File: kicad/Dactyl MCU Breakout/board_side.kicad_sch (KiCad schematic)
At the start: 19 parts, among them J11 Columns, J12 Thumbs, J13 Rows, J14 Extrernal, J15 Split, J16 JST, J9 Display, SW4 LED, SW5 Reset, SW6 Battery, U3 Nice!Nano/2040, U4 74HC595

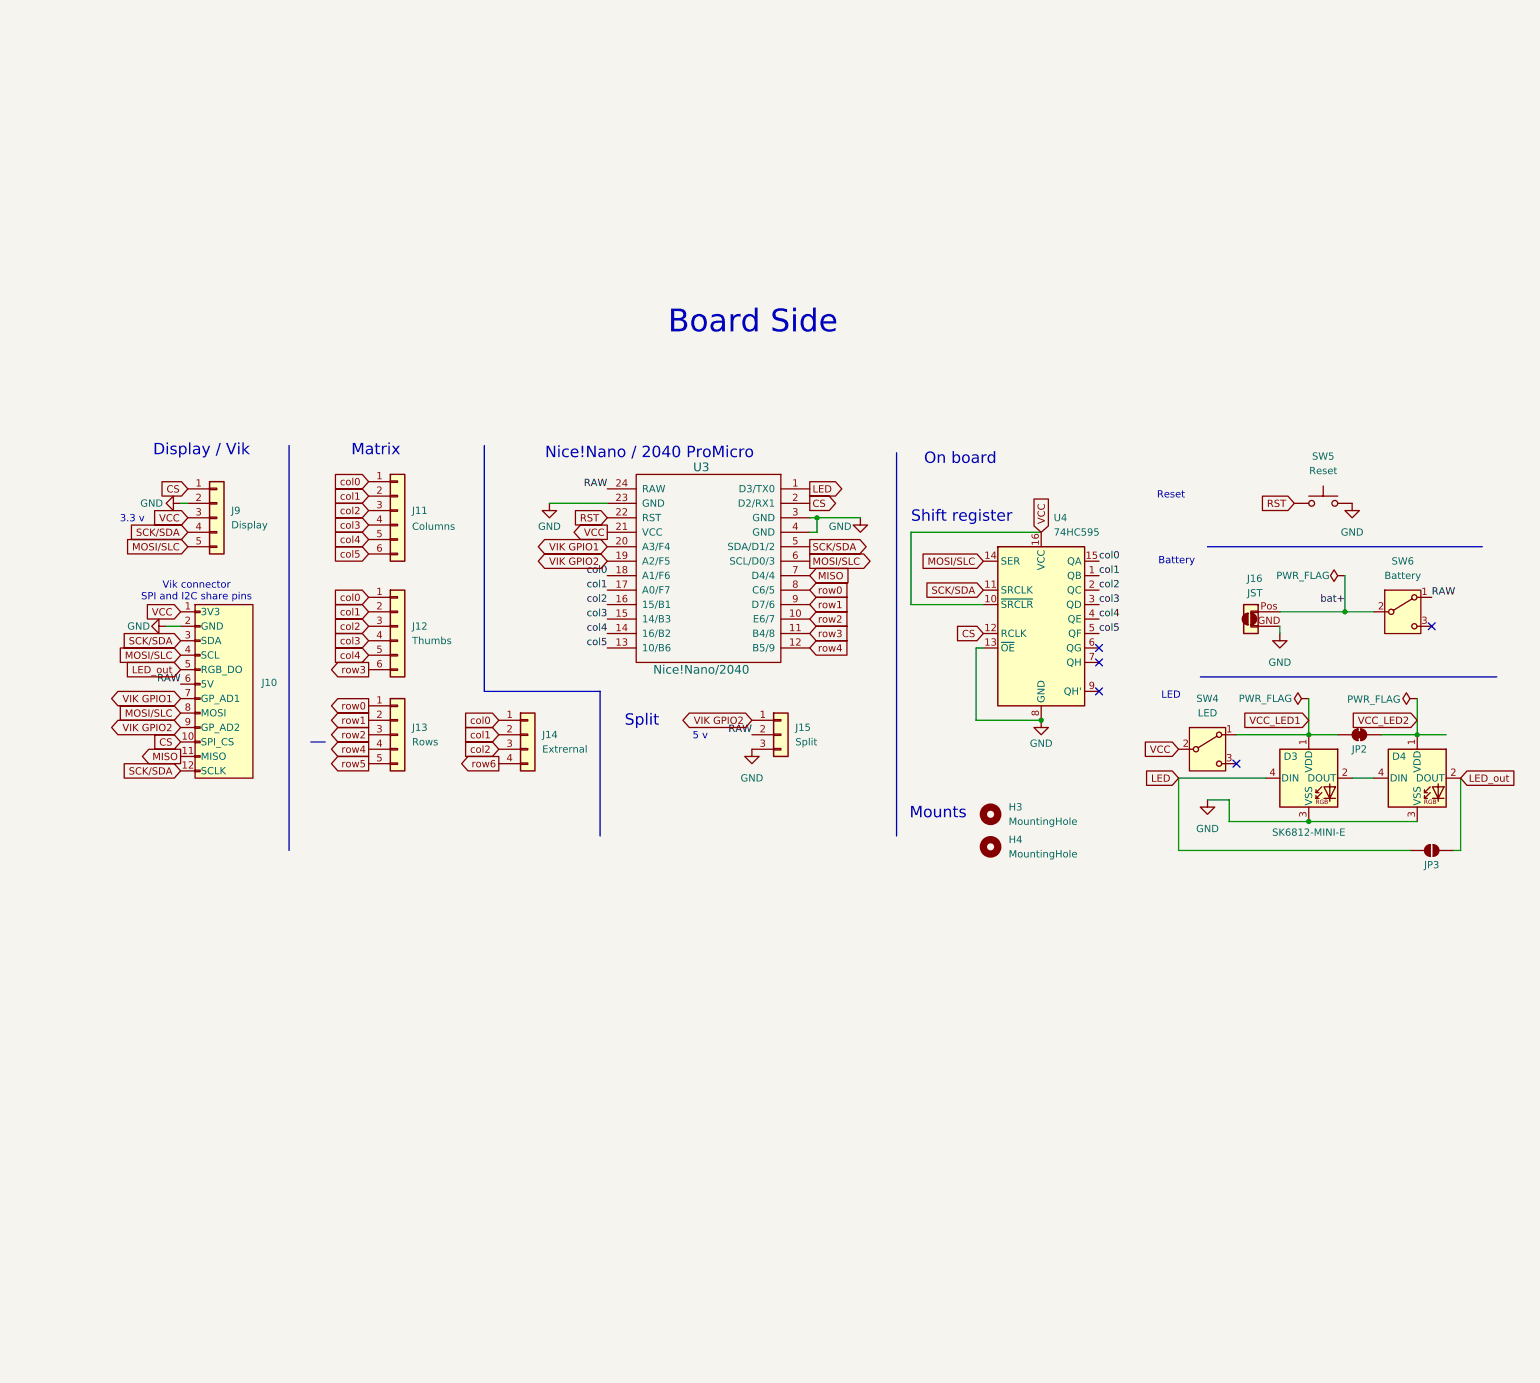
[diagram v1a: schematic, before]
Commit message: feat: bus SPI0, mum/2040 split steal form Vik
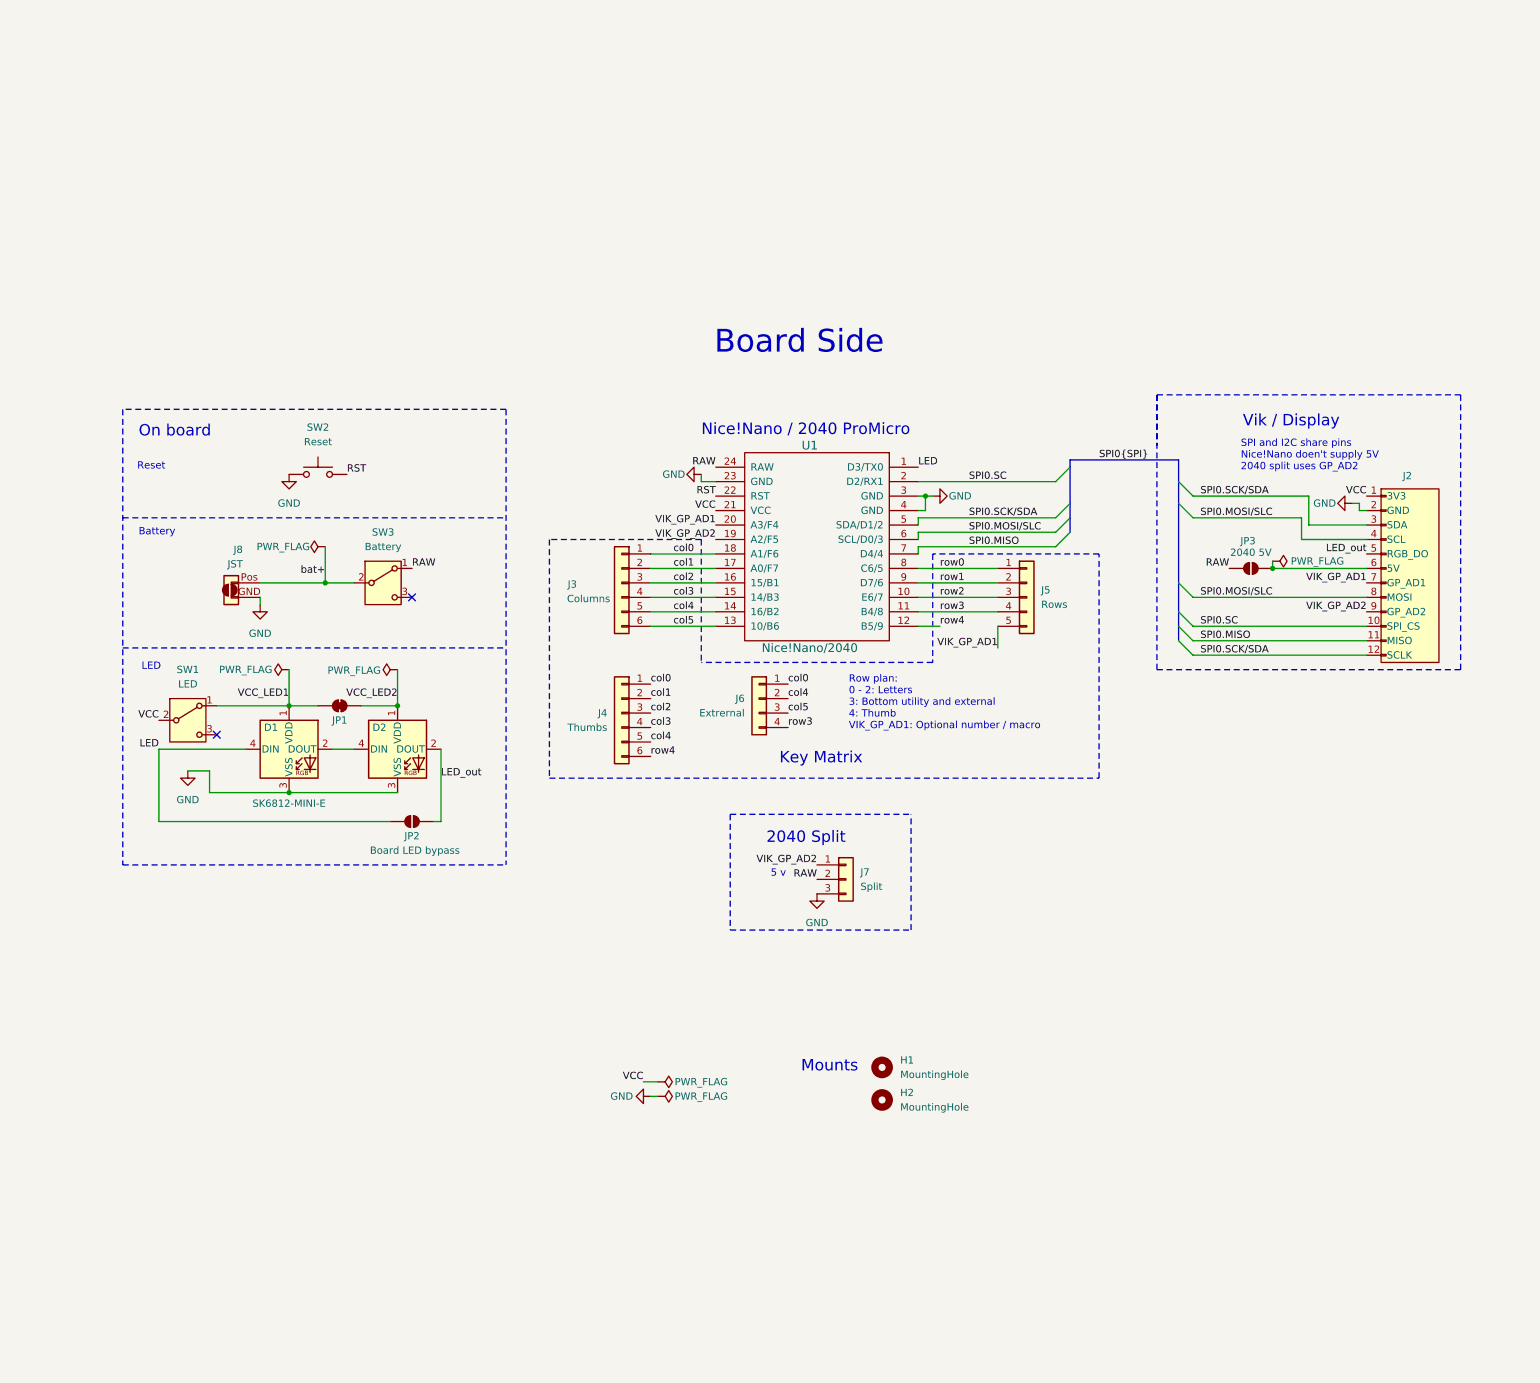
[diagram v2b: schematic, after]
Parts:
- removed D3, D4: SK6812-MINI-E, Dactyl:SK6812-MINI-E-Dog2, symbol Dactyl:SK6812-MINI-E
- removed H3, H4: MountingHole, MountingHole:MountingHole_3.2mm_M3_DIN965_Pad, symbol Mechanical:MountingHole
- removed J10: ~, symbol Dactyl:vik-keyboard-connector
- removed J11: Columns, Connector_PinHeader_2.54mm:PinHeader_1x06_P2.54mm_Vertical, symbol Connector_Generic:Conn_01x06
- removed J12: Thumbs, Connector_PinHeader_2.54mm:PinHeader_1x06_P2.54mm_Vertical, symbol Connector_Generic:Conn_01x06
- removed J13: Rows, Connector_PinHeader_2.54mm:PinHeader_1x05_P2.54mm_Vertical, symbol Connector_Generic:Conn_01x05
- removed J14: Extrernal, Connector_PinHeader_2.54mm:PinHeader_1x04_P2.54mm_Vertical, symbol Connector_Generic:Conn_01x04
- removed J15: Split, Connector_PinHeader_2.54mm:PinHeader_1x03_P2.54mm_Vertical, symbol Connector_Generic:Conn_01x03
- removed J16: JST, Dactyl:JST_PH_S2B-PH-K_1x02_P2.00mm_Horizontal, symbol Dactyl:Conn_01x02_Jump_Two_Side
- removed J9: Display, Connector_PinHeader_2.54mm:PinHeader_1x05_P2.54mm_Vertical, symbol Connector_Generic:Conn_01x05
- removed JP2: LED2 cutoff, Jumper:SolderJumper-2_P1.3mm_Bridged_RoundedPad1.0x1.5mm, symbol Jumper:SolderJumper_2_Bridged
- removed SW4: LED, Dactyl:SW_SPDT_JS202011AQN_wider, symbol Switch:SW_SPDT
- removed SW5: Reset, Dactyl:SW_Tactile_SKHL_Angled, symbol Switch:SW_Push
- removed SW6: Battery, Dactyl:SW_SPDT_JS202011AQN_wider, symbol Switch:SW_SPDT
- removed U3: Nice!Nano/2040, Dactyl:ProMicro_unrouted, symbol Dactyl:ProMicro_r
- removed U4: 74HC595, symbol 74xx:74HC595
- added D1, D2: SK6812-MINI-E, Dactyl:SK6812-MINI-E-Dog2, symbol Dactyl:SK6812-MINI-E
- added H1, H2: MountingHole, MountingHole:MountingHole_3.2mm_M3_DIN965_Pad, symbol Mechanical:MountingHole
- added J2: ~, symbol Dactyl:vik-keyboard-connector
- added J3: Columns, Connector_PinHeader_2.54mm:PinHeader_1x06_P2.54mm_Vertical, symbol Connector_Generic:Conn_01x06
- added J4: Thumbs, Connector_PinHeader_2.54mm:PinHeader_1x06_P2.54mm_Vertical, symbol Connector_Generic:Conn_01x06
- added J5: Rows, Connector_PinHeader_2.54mm:PinHeader_1x05_P2.54mm_Vertical, symbol Connector_Generic:Conn_01x05
- added J6: Extrernal, Connector_PinHeader_2.54mm:PinHeader_1x04_P2.54mm_Vertical, symbol Connector_Generic:Conn_01x04
- added J7: Split, Connector_PinHeader_2.54mm:PinHeader_1x03_P2.54mm_Vertical, symbol Connector_Generic:Conn_01x03
- added J8: JST, Dactyl:JST_PH_S2B-PH-K_1x02_P2.00mm_Horizontal, symbol Dactyl:Conn_01x02_Jump_Two_Side
- added JP1: LED2 cutoff, Jumper:SolderJumper-2_P1.3mm_Bridged_RoundedPad1.0x1.5mm, symbol Jumper:SolderJumper_2_Bridged
- added JP2: Board LED bypass, Jumper:SolderJumper-2_P1.3mm_Bridged_RoundedPad1.0x1.5mm, symbol Jumper:SolderJumper_2_Open
- added SW1: LED, Dactyl:SW_SPDT_JS202011AQN_wider, symbol Switch:SW_SPDT
- added SW2: Reset, Dactyl:SW_Tactile_SKHL_Angled, symbol Switch:SW_Push
- added SW3: Battery, Dactyl:SW_SPDT_JS202011AQN_wider, symbol Switch:SW_SPDT
- added U1: Nice!Nano/2040, Dactyl:ProMicro_unrouted, symbol Dactyl:ProMicro_r
- JP3: value LED2 cutoff -> 2040 5V
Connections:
- net GND: now also D1.3 (VSS), D2.3 (VSS), J2.2 (GND), J7.3 (Pin_3), J8.GND, SW2.2, U1.23 (GND), U1.3 (GND), U1.4 (GND)
- net LED: now also D1.4 (DIN), JP2.1 (A), U1.1 (D3/TX0); no longer JP3.1 (A)
- net LED_out: now also D2.2 (DOUT), J2.5 (RGB_DO), JP2.2 (B); no longer JP3.2 (B)
- net RAW: now also JP3.1 (A), J7.2 (Pin_2), SW3.1 (A), U1.24 (RAW)
- net RST: now also SW2.1, U1.22 (RST)
- net VCC: now also J2.1 (3V3), SW1.2 (B), U1.21 (VCC)
- net VCC_LED1: now also D1.1 (VDD), JP1.1 (A), SW1.1 (A)
- net VCC_LED2: now also D2.1 (VDD), JP1.2 (B)
- net bat+: now also J8.Pos, SW3.2 (B)
- net col0: now also J3.1 (Pin_1), J4.1 (Pin_1), J6.1 (Pin_1), U1.18 (A1/F6)
- net col1: now also J3.2 (Pin_2), J4.2 (Pin_2), U1.17 (A0/F7)
- net col2: now also J3.3 (Pin_3), J4.3 (Pin_3), U1.16 (15/B1)
- net col3: now also J3.4 (Pin_4), J4.4 (Pin_4), U1.15 (14/B3)
- net col4: now also J3.5 (Pin_5), J4.5 (Pin_5), J6.2 (Pin_2), U1.14 (16/B2)
- net col5: now also J3.6 (Pin_6), J6.3 (Pin_3), U1.13 (10/B6)
- net row0: now also J5.1 (Pin_1), U1.8 (C6/5)
- net row1: now also J5.2 (Pin_2), U1.9 (D7/6)
- net row2: now also J5.3 (Pin_3), U1.10 (E6/7)
- net row3: now also J5.4 (Pin_4), J6.4 (Pin_4), U1.11 (B4/8)
- net row4: now also J4.6 (Pin_6), U1.12 (B5/9)
- new net: J2.6 (5V), JP3.2 (B)
- new net: D1.2 (DOUT), D2.4 (DIN)
- new net SPI0.MISO: J2.11 (MISO), U1.7 (D4/4)
- new net SPI0.MOSI/SLC: J2.4 (SCL), J2.8 (MOSI), U1.6 (SCL/D0/3)
- new net SPI0.SC: J2.10 (SPI_CS), U1.2 (D2/RX1)
- new net SPI0.SCK/SDA: J2.12 (SCLK), J2.3 (SDA), U1.5 (SDA/D1/2)
- new net VIK_GP_AD1: J2.7 (GP_AD1), J5.5 (Pin_5), U1.20 (A3/F4)
- new net VIK_GP_AD2: J2.9 (GP_AD2), J7.1 (Pin_1), U1.19 (A2/F5)
- no-connect marks 5 -> 2
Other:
- note added: "2040 Split"
- note added: "Key Matrix"
- note added: "Row plan: 0 - 2: Letters 3: Bottom utility and external 4: Thumb VIK_GP_AD1: Optional number / macro"
- note added: "SPI and I2C share pins Nice!Nano doen't supply 5V 2040 split uses GP_AD2"
- note added: "Vik / Display"
- note removed: "3.3 v"
- note removed: "Display / Vik"
- note removed: "Matrix"
- note removed: "Shift register"
- note removed: "Split"
- note removed: "Vik connector SPI and I2C share pins"
